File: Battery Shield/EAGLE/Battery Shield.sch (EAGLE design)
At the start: 29 parts, among them IC1 MCP73871, U1 TPS61200

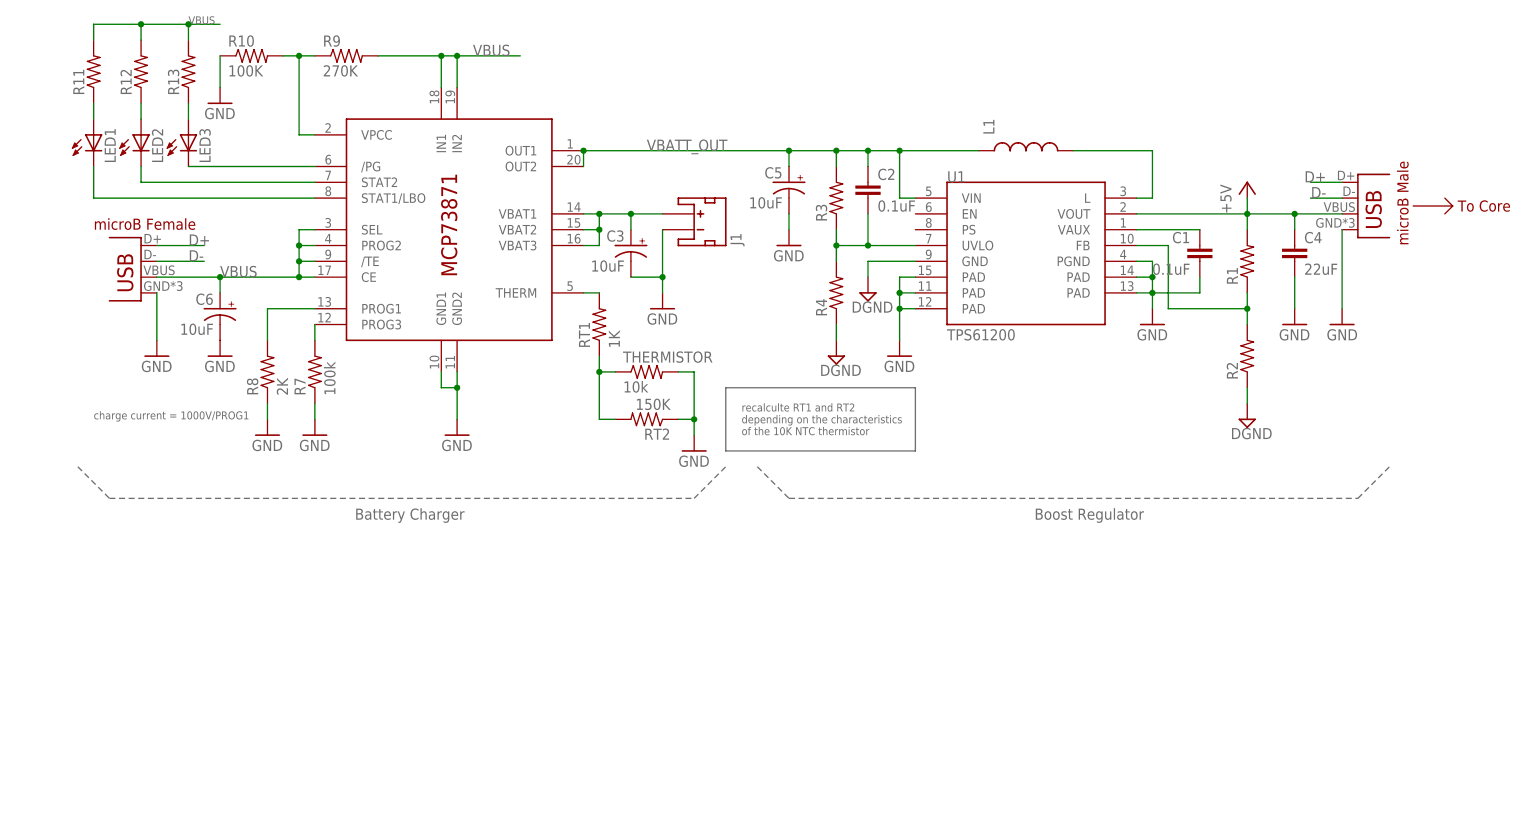
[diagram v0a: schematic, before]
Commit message: updated the battery shield and created the BOM
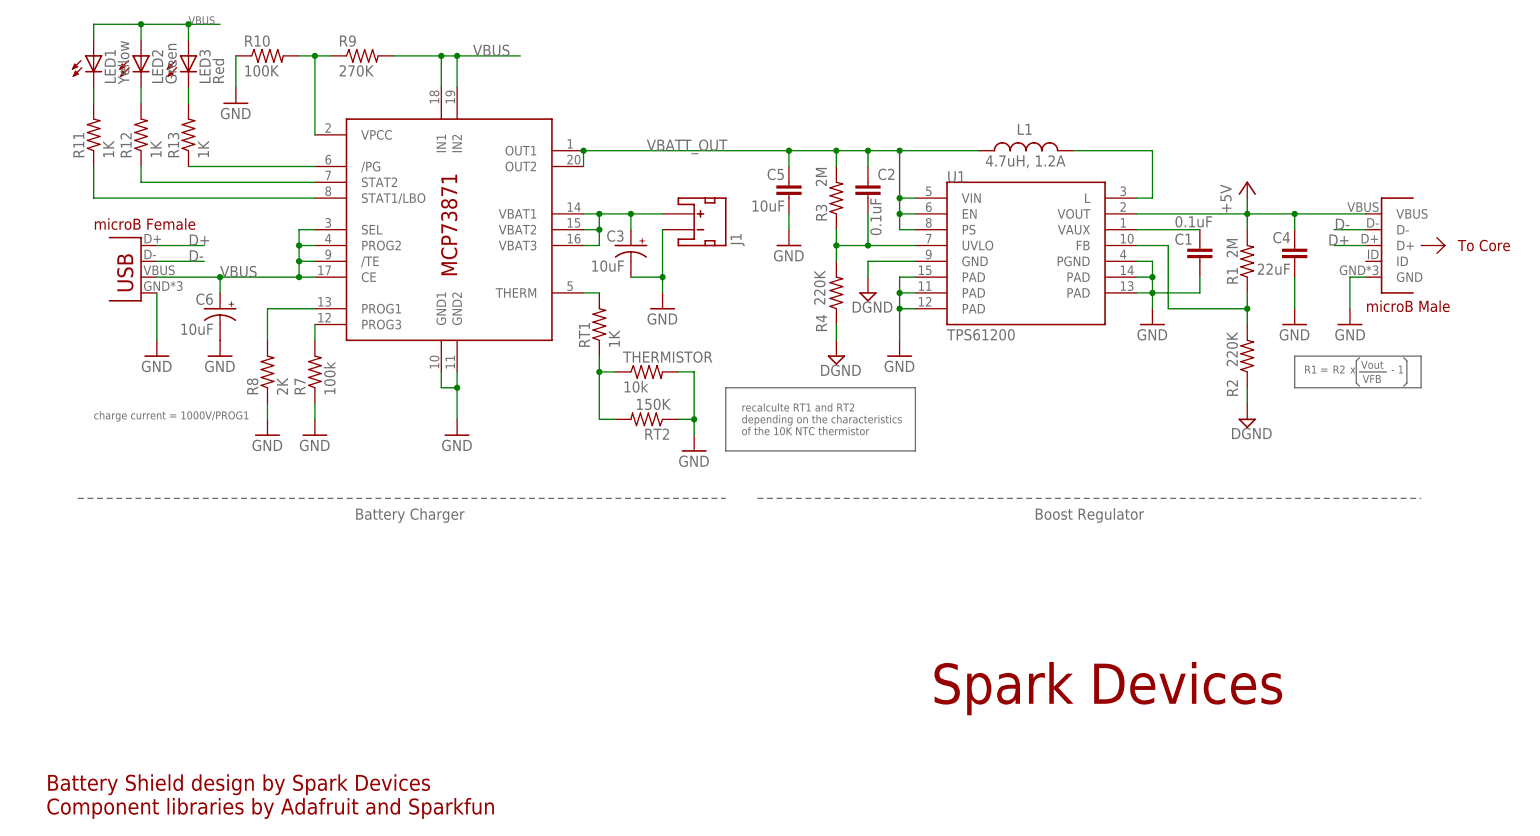
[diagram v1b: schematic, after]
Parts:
- removed JP2, JP3: USB-MICROB, SparkFun-Connectors:USB-MICROB
- added JP1: USBUSB-MICROB-SLOT-HOLE, Spark:USBUSB-MICROB-SLOT-HOLE
- added U$1: USB_MALE, Spark:USB_MALE
- C5: device SparkFun-Capacitors:10UF-16V-10%(TANT) -> SparkFun-Capacitors:CAP1206; PROD_ID CAP-00811 -> (none); VALUE 10uF -> (none)
- L1: value (none) -> 4.7uH, 1.2A
- LED1: value (none) -> Yellow
- LED2: value (none) -> Green
- LED3: value (none) -> Red
- R1, R3: value (none) -> 2M
- R11, R12, R13: value (none) -> 1K
- R2, R4: value (none) -> 220K
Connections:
- removed net N$17: IC1.STAT1/LBO, LED1.C
- new net N$16: LED3.C, R13.2
- net +5V: now also U$1.VBUS; no longer JP3.VBUS
- net D+: now also JP1.D+, U$1.D+; no longer JP2.D+, JP3.D+
- net D-: now also JP1.D-, U$1.D-; no longer JP2.D-, JP3.D-
- net GND: now also C5.2, JP1.GND, U$1.GND; no longer C5.-, JP2.GND, JP3.GND
- net N$10: now also LED2.C, R12.2; no longer LED3.A, R13.1
- net N$14: now also R12.1; no longer LED2.C
- net N$15: now also R13.1; no longer LED3.C
- net N$6: now also IC1.STAT1/LBO; no longer LED1.A
- net N$8: now also LED1.C, R11.2; no longer LED2.A, R12.1
- net VBATT_OUT: now also C5.1, U1.EN, U1.PS; no longer C5.+
- net VBUS: now also JP1.VBUS, LED1.A, LED2.A, LED3.A; no longer JP2.VBUS, R11.2, R12.2, R13.2
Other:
- note added: "- 1"
- note added: "Battery Shield design by Spark Devices Component libraries by Adafruit and Sparkfun"
- note added: "R1 ="
- note added: "R2"
- note added: "Spark Devices"
- note added: "VFB"
- note added: "Vout"
- note added: "x"
- moved on the sheet: LED1, LED2, LED3, R10, R11, R12, R13, R9

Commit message: updated shield BOMs and boards
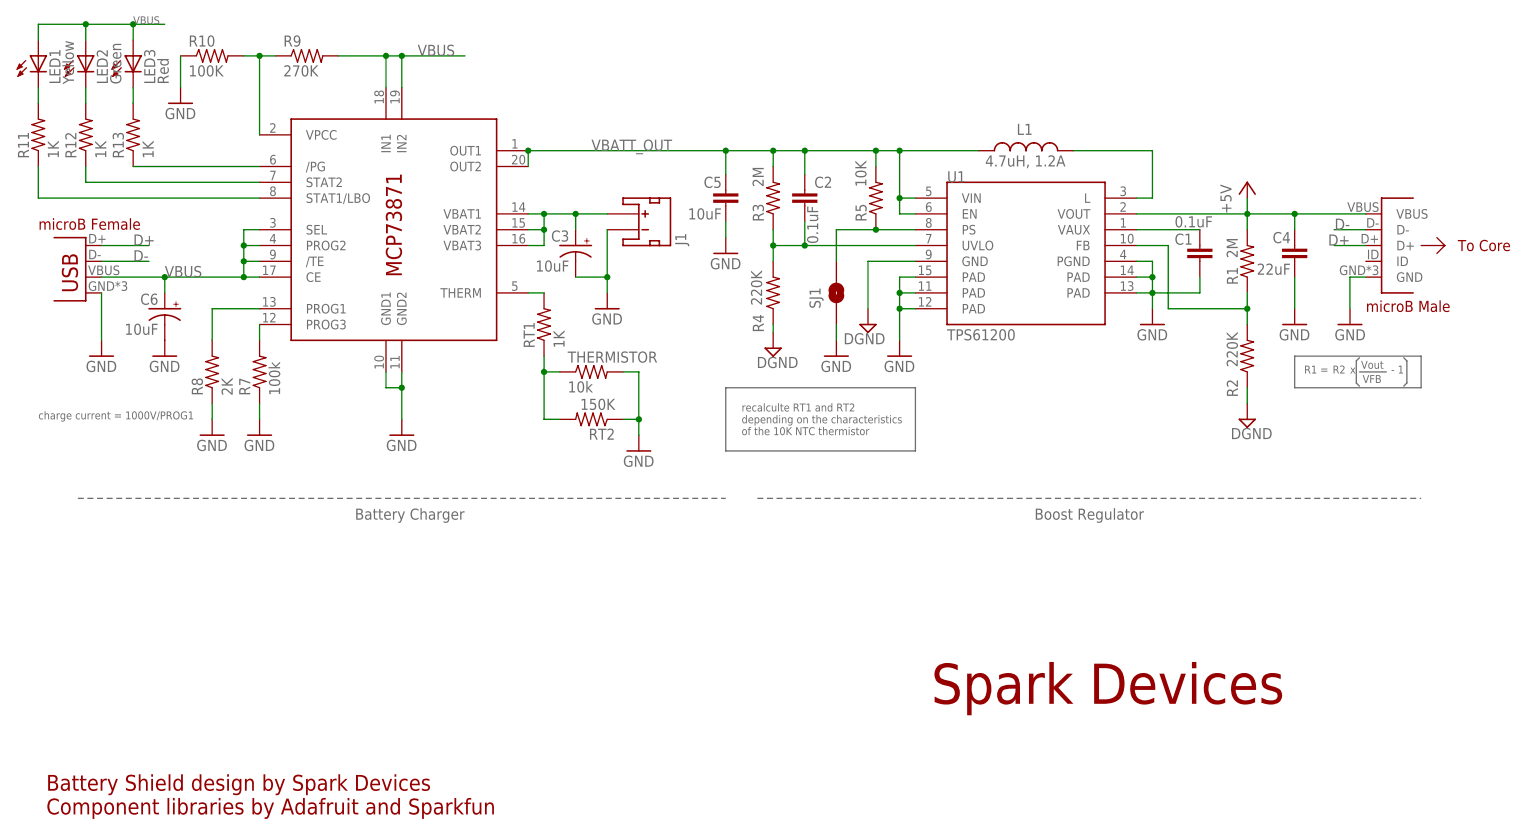
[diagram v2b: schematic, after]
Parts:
- added R5: 10K, SparkFun-Passives:RESISTOR0402-RES
- added SJ1: SOLDERJUMPERNO, SparkFun-Passives:SOLDERJUMPERNO
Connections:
- new net N$19: R5.1, SJ1.2, U1.PS
- net GND: now also SJ1.1
- net VBATT_OUT: now also R5.2; no longer U1.PS
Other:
- moved on the sheet: C2, C3, C5, C6, J1, LED1, LED2, LED3, R10, R11, R12, R13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

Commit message: updated changes to the battery shield
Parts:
- removed THERMISTOR: 10k, rcl:R-US_R0805
- added R6: 10K, SparkFun-Passives:RESISTOR0402-RES
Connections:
- net GND: now also R6.1; no longer THERMISTOR.2
- net N$7: now also R6.2; no longer THERMISTOR.1
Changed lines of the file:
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@@
 <setting verticaltext="up"/>
 </settings>
-<grid distance="0.05" unitdist="inch" unit="inch" style="lines" multiple="1" display="yes" altdistance="0.01" altunitdist="inch" altunit="inch"/>
+<grid distance="0.05" unitdist="inch" unit="inch" style="lines" multiple="1" display="no" altdistance="0.01" altunitdist="inch" altunit="inch"/>
 <layers>
 <layer number="1" name="Top" color="4" fill="1" visible="no" active="no"/>
@@
 <part name="C3" library="SparkFun-Capacitors" deviceset="10UF-16V-10%(TANT)" device="" value="10uF"/>
 <part name="GND12" library="supply1" deviceset="GND" device=""/>
-<part name="THERMISTOR" library="rcl" deviceset="R-US_" device="R0805" value="10k"/>
 <part name="LED1" library="SparkFun-LED" deviceset="LED" device="0603" value="Yellow"/>
 <part name="LED2" library="SparkFun-LED" deviceset="LED" device="0603" value="Green"/>
@@
 <part name="R5" library="SparkFun-Passives" deviceset="RESISTOR" device="0402-RES" value="10K"/>
 <part name="GND14" library="supply1" deviceset="GND" device=""/>
+<part name="R6" library="SparkFun-Passives" deviceset="RESISTOR" device="0402-RES" value="10K"/>
 </parts>
 <sheets>
@@
 <instance part="C3" gate="G$1" x="92.71" y="99.06" rot="MR0"/>
 <instance part="GND12" gate="1" x="116.84" y="97.79"/>
-<instance part="THERMISTOR" gate="G$1" x="95.25" y="78.74"/>
 <instance part="LED1" gate="G$1" x="6.35" y="129.54"/>
 <instance part="LED2" gate="G$1" x="13.97" y="129.54"/>
@@
 </instance>
 <instance part="GND14" gate="1" x="134.62" y="81.28"/>
+<instance part="R6" gate="G$1" x="95.25" y="78.74" smashed="yes" rot="R180">
+<attribute name="NAME" x="101.6" y="82.3214" size="1.778" layer="95" rot="R180"/>
+<attribute name="VALUE" x="97.282" y="82.296" size="1.778" layer="96" rot="R180"/>
+</instance>
 </instances>
 <busses>
@@
 </segment>
 <segment>
-<pinref part="THERMISTOR" gate="G$1" pin="2"/>
 <pinref part="GND7" gate="1" pin="GND"/>
 <wire x1="100.33" y1="78.74" x2="102.87" y2="78.74" width="0.1524" layer="91"/>
@@
 <wire x1="100.33" y1="71.12" x2="102.87" y2="71.12" width="0.1524" layer="91"/>
 <junction x="102.87" y="71.12"/>
+<pinref part="R6" gate="G$1" pin="1"/>
 </segment>
 <segment>
@@
 <pinref part="RT1" gate="G$1" pin="1"/>
 <wire x1="87.63" y1="81.28" x2="87.63" y2="78.74" width="0.1524" layer="91"/>
-<pinref part="THERMISTOR" gate="G$1" pin="1"/>
 <wire x1="87.63" y1="78.74" x2="90.17" y2="78.74" width="0.1524" layer="91"/>
 <pinref part="RT2" gate="G$1" pin="2"/>
@@
 <wire x1="87.63" y1="71.12" x2="87.63" y2="78.74" width="0.1524" layer="91"/>
 <junction x="87.63" y="78.74"/>
-</segment>
-</net>
+<pinref part="R6" gate="G$1" pin="2"/>
+</segment>
+</net>

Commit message: updated battery shield
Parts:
- removed U$1: USB_MALE, Spark:USB_MALE
- added JP2: USBFCI, Spark:USBFCI
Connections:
- net +5V: now also JP2.VBUS; no longer U$1.VBUS
- net D+: now also JP2.D+; no longer U$1.D+
- net D-: now also JP2.D-; no longer U$1.D-
- net GND: now also JP2.GND; no longer U$1.GND
